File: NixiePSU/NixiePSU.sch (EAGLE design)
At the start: 18 parts, among them IC1 NE555, Q1 BUZ11BV, T1 BC547

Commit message: Swap some components.
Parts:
- C3: device rcl:C-US025-024X044 -> rcl:CPOL-USE5-13
- R1, R2, R3, R4, R5, R6: device rcl:R-US_0204/5 -> rcl:R-US_0207/7
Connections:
- net GND: now also C3.-; no longer C3.2
- net N$9: now also C3.+; no longer C3.1
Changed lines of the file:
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@@
 <?xml version="1.0" encoding="utf-8"?>
 <!DOCTYPE eagle SYSTEM "eagle.dtd">
-<eagle version="7.7.0">
+<eagle version="8.2.0">
 <drawing>
 <settings>
@@
 <part name="L1" library="Inductors" deviceset="L-US" device="" value="100uH"/>
 <part name="GND1" library="supply1" deviceset="GND" device=""/>
-<part name="R1" library="rcl" deviceset="R-US_" device="0204/5" value="56k"/>
-<part name="R2" library="rcl" deviceset="R-US_" device="0204/5" value="10k"/>
-<part name="R3" library="rcl" deviceset="R-US_" device="0204/5" value="1k"/>
+<part name="R1" library="rcl" deviceset="R-US_" device="0207/7" value="56k"/>
+<part name="R2" library="rcl" deviceset="R-US_" device="0207/7" value="10k"/>
+<part name="R3" library="rcl" deviceset="R-US_" device="0207/7" value="1k"/>
 <part name="D1" library="diode" deviceset="1N4942" device=""/>
 <part name="P+1" library="supply1" deviceset="VCC" device=""/>
 <part name="P+2" library="supply1" deviceset="VCC" device=""/>
 <part name="P+3" library="supply1" deviceset="VCC" device=""/>
-<part name="R4" library="rcl" deviceset="R-US_" device="0204/5" value="470"/>
-<part name="R5" library="rcl" deviceset="R-US_" device="0204/5" value="220k"/>
+<part name="R4" library="rcl" library_urn="urn:adsk.eagle:library:334" deviceset="R-US_" device="0207/7" value="470"/>
+<part name="R5" library="rcl" deviceset="R-US_" device="0207/7" value="220k"/>
 <part name="X1" library="con-wago-508" deviceset="W237-02P" device=""/>
 <part name="VR1" library="pot" deviceset="TRIM_US-" device="B25P"/>
@@
 <part name="GND3" library="supply1" deviceset="GND" device=""/>
 <part name="GND4" library="supply1" deviceset="GND" device=""/>
-<part name="C3" library="rcl" deviceset="C-US" device="025-024X044" value="100pF"/>
-<part name="R6" library="rcl" deviceset="R-US_" device="0204/5" value="2k2"/>
+<part name="C3" library="rcl" library_urn="urn:adsk.eagle:library:334" deviceset="CPOL-US" device="E5-13" value="100pF"/>
+<part name="R6" library="rcl" deviceset="R-US_" device="0207/7" value="2k2"/>
 <part name="GND5" library="supply1" deviceset="GND" device=""/>
 <part name="C4" library="rcl" deviceset="CPOL-US" device="E3.5-8" value="4u7"/>
@@
 </segment>
 <segment>
-<pinref part="C3" gate="G$1" pin="2"/>
+<pinref part="C3" gate="G$1" pin="-"/>
 <wire x1="101.6" y1="58.42" x2="101.6" y2="15.24" width="0.1524" layer="91"/>
 <pinref part="GND5" gate="1" pin="GND"/>
@@
 <segment>
 <pinref part="R6" gate="G$1" pin="1"/>
-<pinref part="C3" gate="G$1" pin="1"/>
+<pinref part="C3" gate="G$1" pin="+"/>
 <wire x1="101.6" y1="71.12" x2="101.6" y2="66.04" width="0.1524" layer="91"/>
 </segment>
@@
 </schematic>
 </drawing>
+<compatibility>
+<note version="8.2" severity="warning">
+Since Version 8.2, Eagle supports online libraries. The ids
+of those online libraries will not be understood (or retained)
+with this version.
+</note>
+</compatibility>
 </eagle>

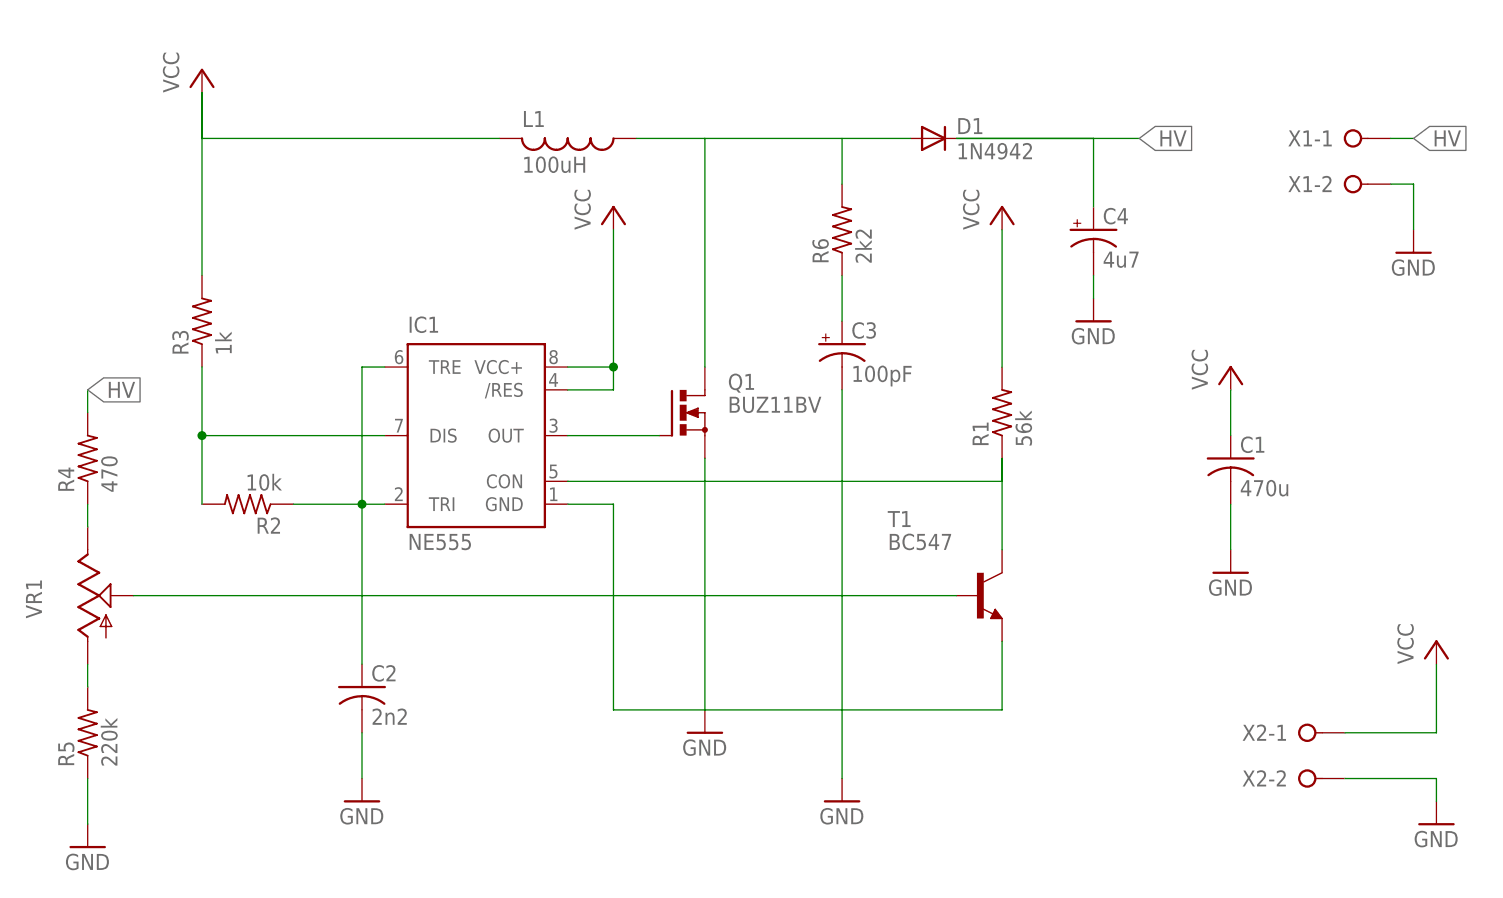
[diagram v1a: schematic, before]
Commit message: Rewire the threshold pin on the 555. Fix some ERC errors.
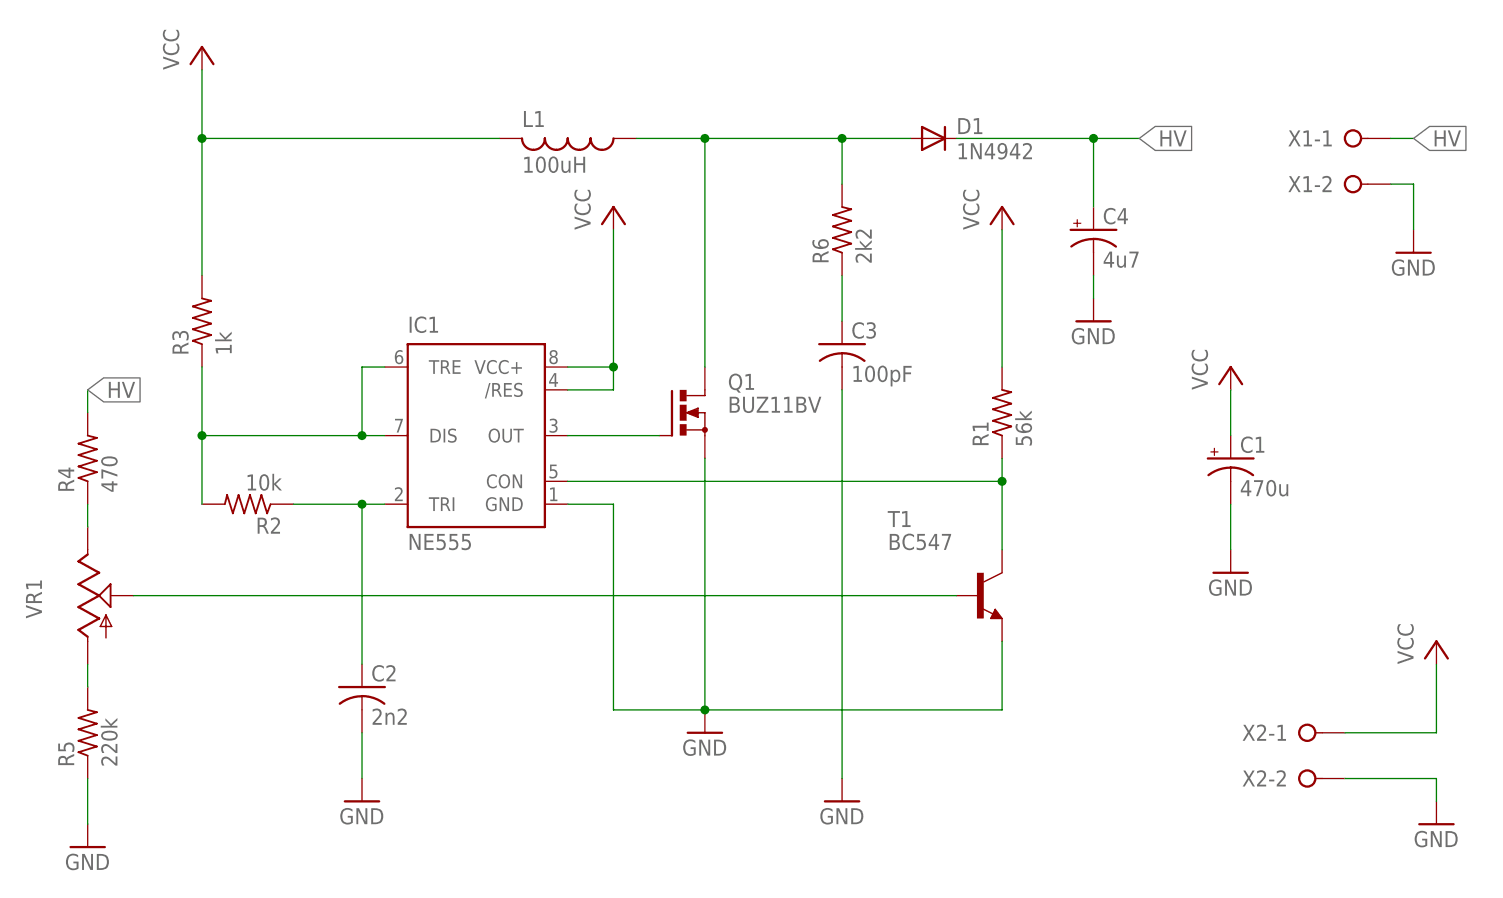
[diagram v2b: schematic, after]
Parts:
- C1: device rcl:C-US025-024X044 -> rcl:CPOL-USE5-13
- C2: device rcl:C-US025-024X044 -> rcl:C-US050-025X075
- C3: device rcl:CPOL-USE5-13 -> rcl:C-US050-025X075
- R1, R2, R3, R4, R5, R6: device rcl:R-US_0207/7 -> rcl:R-US_0207/10
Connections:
- net GND: now also C1.-, C3.2; no longer C1.2, C3.-
- net N$10: no longer IC1.TRE
- net N$3: now also IC1.TRE
- net N$9: now also C3.1; no longer C3.+
- net VCC: now also C1.+; no longer C1.1
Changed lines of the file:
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@@
 <?xml version="1.0" encoding="utf-8"?>
 <!DOCTYPE eagle SYSTEM "eagle.dtd">
-<eagle version="8.2.0">
+<eagle version="8.2.2">
 <drawing>
 <settings>
@@
 <part name="L1" library="Inductors" deviceset="L-US" device="" value="100uH"/>
 <part name="GND1" library="supply1" deviceset="GND" device=""/>
-<part name="R1" library="rcl" deviceset="R-US_" device="0207/7" value="56k"/>
-<part name="R2" library="rcl" deviceset="R-US_" device="0207/7" value="10k"/>
-<part name="R3" library="rcl" deviceset="R-US_" device="0207/7" value="1k"/>
+<part name="R1" library="rcl" deviceset="R-US_" device="0207/10" value="56k"/>
+<part name="R2" library="rcl" deviceset="R-US_" device="0207/10" value="10k"/>
+<part name="R3" library="rcl" deviceset="R-US_" device="0207/10" value="1k"/>
 <part name="D1" library="diode" deviceset="1N4942" device=""/>
 <part name="P+1" library="supply1" deviceset="VCC" device=""/>
 <part name="P+2" library="supply1" deviceset="VCC" device=""/>
 <part name="P+3" library="supply1" deviceset="VCC" device=""/>
-<part name="R4" library="rcl" library_urn="urn:adsk.eagle:library:334" deviceset="R-US_" device="0207/7" value="470"/>
-<part name="R5" library="rcl" deviceset="R-US_" device="0207/7" value="220k"/>
+<part name="R4" library="rcl" deviceset="R-US_" device="0207/10" value="470"/>
+<part name="R5" library="rcl" deviceset="R-US_" device="0207/10" value="220k"/>
 <part name="X1" library="con-wago-508" deviceset="W237-02P" device=""/>
 <part name="VR1" library="pot" deviceset="TRIM_US-" device="B25P"/>
 <part name="GND2" library="supply1" deviceset="GND" device=""/>
-<part name="C1" library="rcl" deviceset="C-US" device="025-024X044" value="470u"/>
-<part name="C2" library="rcl" deviceset="C-US" device="025-024X044" value="2n2"/>
+<part name="C1" library="rcl" deviceset="CPOL-US" device="E5-13" value="470u"/>
+<part name="C2" library="rcl" deviceset="C-US" device="050-025X075" value="2n2"/>
 <part name="P+4" library="supply1" deviceset="VCC" device=""/>
 <part name="GND3" library="supply1" deviceset="GND" device=""/>
 <part name="GND4" library="supply1" deviceset="GND" device=""/>
-<part name="C3" library="rcl" library_urn="urn:adsk.eagle:library:334" deviceset="CPOL-US" device="E5-13" value="100pF"/>
-<part name="R6" library="rcl" deviceset="R-US_" device="0207/7" value="2k2"/>
+<part name="C3" library="rcl" deviceset="C-US" device="050-025X075" value="100pF"/>
+<part name="R6" library="rcl" deviceset="R-US_" device="0207/10" value="2k2"/>
 <part name="GND5" library="supply1" deviceset="GND" device=""/>
 <part name="C4" library="rcl" deviceset="CPOL-US" device="E3.5-8" value="4u7"/>
@@
 <instance part="R3" gate="G$1" x="30.48" y="66.04" rot="R90"/>
 <instance part="D1" gate="1" x="111.76" y="86.36"/>
-<instance part="P+1" gate="VCC" x="30.48" y="93.98"/>
+<instance part="P+1" gate="VCC" x="30.48" y="96.52"/>
 <instance part="P+2" gate="VCC" x="119.38" y="78.74"/>
 <instance part="P+3" gate="VCC" x="76.2" y="78.74"/>
@@
 <pinref part="IC1" gate="G$1" pin="DIS"/>
 <pinref part="R3" gate="G$1" pin="1"/>
-<wire x1="50.8" y1="53.34" x2="30.48" y2="53.34" width="0.1524" layer="91"/>
+<wire x1="50.8" y1="53.34" x2="48.26" y2="53.34" width="0.1524" layer="91"/>
+<wire x1="48.26" y1="53.34" x2="30.48" y2="53.34" width="0.1524" layer="91"/>
 <wire x1="30.48" y1="53.34" x2="30.48" y2="60.96" width="0.1524" layer="91"/>
 <pinref part="R2" gate="G$1" pin="2"/>
 <wire x1="30.48" y1="45.72" x2="30.48" y2="53.34" width="0.1524" layer="91"/>
 <junction x="30.48" y="53.34"/>
+<pinref part="IC1" gate="G$1" pin="TRE"/>
+<wire x1="50.8" y1="60.96" x2="48.26" y2="60.96" width="0.1524" layer="91"/>
+<wire x1="48.26" y1="60.96" x2="48.26" y2="53.34" width="0.1524" layer="91"/>
+<junction x="48.26" y="53.34"/>
 </segment>
 </net>
 <net name="VCC" class="0">
-<segment>
-<pinref part="R3" gate="G$1" pin="2"/>
-<wire x1="30.48" y1="71.12" x2="30.48" y2="91.44" width="0.1524" layer="91"/>
-<pinref part="P+1" gate="VCC" pin="VCC"/>
-<pinref part="L1" gate="G$1" pin="2"/>
-<wire x1="63.5" y1="86.36" x2="30.48" y2="86.36" width="0.1524" layer="91"/>
-<wire x1="30.48" y1="86.36" x2="30.48" y2="91.44" width="0.1524" layer="91"/>
-</segment>
 <segment>
 <pinref part="R1" gate="G$1" pin="2"/>
@@
 <segment>
 <pinref part="P+4" gate="VCC" pin="VCC"/>
-<pinref part="C1" gate="G$1" pin="1"/>
+<pinref part="C1" gate="G$1" pin="+"/>
 <wire x1="144.78" y1="58.42" x2="144.78" y2="53.34" width="0.1524" layer="91"/>
 </segment>
@@
 <wire x1="167.64" y1="20.32" x2="167.64" y2="27.94" width="0.1524" layer="91"/>
 </segment>
-</net>
-<net name="N$5" class="0">
-<segment>
-<pinref part="IC1" gate="G$1" pin="CON"/>
-<pinref part="R1" gate="G$1" pin="1"/>
-<wire x1="71.12" y1="48.26" x2="119.38" y2="48.26" width="0.1524" layer="91"/>
-<wire x1="119.38" y1="48.26" x2="119.38" y2="50.8" width="0.1524" layer="91"/>
-<pinref part="T1" gate="G$1" pin="C"/>
-<wire x1="119.38" y1="50.8" x2="119.38" y2="40.64" width="0.1524" layer="91"/>
+<segment>
+<pinref part="R3" gate="G$1" pin="2"/>
+<wire x1="30.48" y1="71.12" x2="30.48" y2="86.36" width="0.1524" layer="91"/>
+<pinref part="L1" gate="G$1" pin="2"/>
+<wire x1="63.5" y1="86.36" x2="30.48" y2="86.36" width="0.1524" layer="91"/>
+<pinref part="P+1" gate="VCC" pin="VCC"/>
+<wire x1="30.48" y1="93.98" x2="30.48" y2="86.36" width="0.1524" layer="91"/>
+<junction x="30.48" y="86.36"/>
 </segment>
 </net>
@@
 <wire x1="109.22" y1="86.36" x2="101.6" y2="86.36" width="0.1524" layer="91"/>
 <wire x1="101.6" y1="86.36" x2="101.6" y2="81.28" width="0.1524" layer="91"/>
+<junction x="86.36" y="86.36"/>
+<junction x="101.6" y="86.36"/>
 </segment>
 </net>
@@
 <wire x1="76.2" y1="45.72" x2="76.2" y2="22.86" width="0.1524" layer="91"/>
 <wire x1="76.2" y1="22.86" x2="86.36" y2="22.86" width="0.1524" layer="91"/>
+<junction x="86.36" y="22.86"/>
 </segment>
 <segment>
@@
 </segment>
 <segment>
-<pinref part="C1" gate="G$1" pin="2"/>
+<pinref part="C1" gate="G$1" pin="-"/>
 <pinref part="GND3" gate="1" pin="GND"/>
 <wire x1="144.78" y1="45.72" x2="144.78" y2="40.64" width="0.1524" layer="91"/>
@@
 </segment>
 <segment>
-<pinref part="C3" gate="G$1" pin="-"/>
+<pinref part="C3" gate="G$1" pin="2"/>
 <wire x1="101.6" y1="58.42" x2="101.6" y2="15.24" width="0.1524" layer="91"/>
 <pinref part="GND5" gate="1" pin="GND"/>
@@
 <segment>
 <pinref part="D1" gate="1" pin="C"/>
-<wire x1="114.3" y1="86.36" x2="134.62" y2="86.36" width="0.1524" layer="91"/>
+<wire x1="114.3" y1="86.36" x2="129.54" y2="86.36" width="0.1524" layer="91"/>
 <label x="134.62" y="86.36" size="1.778" layer="95" xref="yes"/>
 <pinref part="C4" gate="G$1" pin="+"/>
-<wire x1="114.3" y1="86.36" x2="129.54" y2="86.36" width="0.1524" layer="91"/>
-<wire x1="129.54" y1="86.36" x2="129.54" y2="78.74" width="0.1524" layer="91"/>
+<wire x1="129.54" y1="86.36" x2="134.62" y2="86.36" width="0.1524" layer="91"/>
+<wire x1="129.54" y1="78.74" x2="129.54" y2="86.36" width="0.1524" layer="91"/>
+<junction x="129.54" y="86.36"/>
 </segment>
 <segment>
@@
 <segment>
 <pinref part="R6" gate="G$1" pin="1"/>
-<pinref part="C3" gate="G$1" pin="+"/>
+<pinref part="C3" gate="G$1" pin="1"/>
 <wire x1="101.6" y1="71.12" x2="101.6" y2="66.04" width="0.1524" layer="91"/>
 </segment>
@@
 <net name="N$10" class="0">
 <segment>
-<pinref part="IC1" gate="G$1" pin="TRE"/>
-<wire x1="48.26" y1="60.96" x2="50.8" y2="60.96" width="0.1524" layer="91"/>
 <pinref part="IC1" gate="G$1" pin="TRI"/>
 <pinref part="C2" gate="G$1" pin="1"/>
 <wire x1="50.8" y1="45.72" x2="48.26" y2="45.72" width="0.1524" layer="91"/>
 <wire x1="48.26" y1="45.72" x2="48.26" y2="27.94" width="0.1524" layer="91"/>
-<wire x1="48.26" y1="60.96" x2="48.26" y2="45.72" width="0.1524" layer="91"/>
 <junction x="48.26" y="45.72"/>
 <pinref part="R2" gate="G$1" pin="1"/>
 <wire x1="40.64" y1="45.72" x2="48.26" y2="45.72" width="0.1524" layer="91"/>
+</segment>
+</net>
+<net name="N$6" class="0">
+<segment>
+<pinref part="T1" gate="G$1" pin="C"/>
+<pinref part="R1" gate="G$1" pin="1"/>
+<wire x1="119.38" y1="50.8" x2="119.38" y2="48.26" width="0.1524" layer="91"/>
+<pinref part="IC1" gate="G$1" pin="CON"/>
+<wire x1="119.38" y1="48.26" x2="119.38" y2="40.64" width="0.1524" layer="91"/>
+<wire x1="71.12" y1="48.26" x2="119.38" y2="48.26" width="0.1524" layer="91"/>
+<junction x="119.38" y="48.26"/>
 </segment>
 </net>
@@
 </schematic>
 </drawing>
-<compatibility>
-<note version="8.2" severity="warning">
-Since Version 8.2, Eagle supports online libraries. The ids
-of those online libraries will not be understood (or retained)
-with this version.
-</note>
-</compatibility>
 </eagle>

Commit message: Bunch of random updated
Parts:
- R4: value 470 -> 470k
- R5: value 220k -> 1k2
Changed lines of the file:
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@@
 <?xml version="1.0" encoding="utf-8"?>
 <!DOCTYPE eagle SYSTEM "eagle.dtd">
-<eagle version="8.2.2">
+<eagle version="7.7.0">
 <drawing>
 <settings>
@@
 <part name="P+2" library="supply1" deviceset="VCC" device=""/>
 <part name="P+3" library="supply1" deviceset="VCC" device=""/>
-<part name="R4" library="rcl" deviceset="R-US_" device="0207/10" value="470"/>
-<part name="R5" library="rcl" deviceset="R-US_" device="0207/10" value="220k"/>
+<part name="R4" library="rcl" deviceset="R-US_" device="0207/10" value="470k"/>
+<part name="R5" library="rcl" deviceset="R-US_" device="0207/10" value="1k2"/>
 <part name="X1" library="con-wago-508" deviceset="W237-02P" device=""/>
 <part name="VR1" library="pot" deviceset="TRIM_US-" device="B25P"/>
